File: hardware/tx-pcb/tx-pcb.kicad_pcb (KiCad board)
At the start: 2 copper layers, 61 parts, among them J1 Conn_To_J1, J2 Conn_To_J2, J3 BLIO, J4 Conn_01x05, J5 Conn_01x04, SW1 BOOT0, SW2 RESET, SW3 BTN1, SW4 BTN2, SW5 BTN3, SW6 BTN4, SW7 BTN5, U1 USBLC6-2SC6, U2 STM32WB55CEUx, X1 CS11336-32M, X2 ABS07-32.768KHZ-1-T

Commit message: progressed on hardware design
progressed on hardware design. completed most of the layout. waiting for pitch of the sx1262 and decision on switching regulator.
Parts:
- C16, C20, C21, C22, C23, C24, R10, R11, R12, R13, R14, SW3, SW4, SW5, SW6, SW7: moved to B.Cu
- R9: moved to F.Cu
- moved C20 134.4 mm to (186.8, 114.4)
- moved SW3 128.9 mm to (184.2, 113.8), turned to 180 degrees
- moved USB1 127.5 mm to (126.0, 90.2), turned to -90 degrees
- moved R2 120.4 mm to (131.9, 90.2), turned to -90 degrees
- moved R10 119.7 mm to (183.0, 111.0), turned to 0 degrees
- moved R1 117.8 mm to (131.4, 86.0), turned to 0 degrees
- moved U1 116.7 mm to (134.9, 90.0), turned to 0 degrees
- moved C21 114.8 mm to (186.8, 129.1)
- moved D1 112.4 mm to (135.0, 86.0), turned to 180 degrees
- moved SW4 109.6 mm to (184.2, 128.8), turned to 180 degrees
- moved J3 104.1 mm to (146.5, 65.0)
- moved R11 100.7 mm to (183.8, 126.0), turned to 0 degrees
- moved C23 97.4 mm to (186.8, 98.9)
- moved L4 97.3 mm to (146.4, 73.2), turned to 90 degrees
- moved C15 95.4 mm to (148.9, 72.0), turned to 0 degrees
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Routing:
- net /BOOT0: track 0.00 -> 57.5 mm, vias 0 -> 2
- net /SWD_NSRT: track 0.00 -> 48.9 mm, vias 0 -> 1
- net /SWCLK: track 0.00 -> 31.1 mm
- net /SWDIO: track 0.00 -> 27.4 mm
- net /I2C1_SCL: track 2.96 -> 23.1 mm
- net /I2C1_SDA: track 2.60 -> 22.2 mm
- net /SX1262_RST: track 0.00 -> 12.5 mm
- net /SX1262_DIO1: track 0.00 -> 11.7 mm
- net /SPI_MOSI: track 0.00 -> 10.7 mm
- net /SP1_MISO: track 0.00 -> 9.91 mm
- net Net-(R5-Pad2): track 0.00 -> 9.57 mm
- net /SPI_SCK: track 0.00 -> 9.08 mm
- net /SX1262_NSS: track 0.00 -> 8.07 mm
- net /USB_DP: track 3.56 -> 10.1 mm
- net /USB_DM: track 3.56 -> 10.1 mm
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- added copper zone on B.Cu, net +3V3
- added copper zone on F.Cu, net +3V3
- added copper zone on In1.Cu, net GND
- added copper zone on In2.Cu, net GND
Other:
- board outline added: 83.4 x 79.1 mm
- copper layers 2 -> 4
- board text added: "BOOT"
- board text added: "RESET"
- board text added: "gnd"
- board text added: "rst"
- board text added: "scl"
- board text added: "sda"
- board text added: "swclk"
- board text added: "swdio"
- board text added: "vcc"

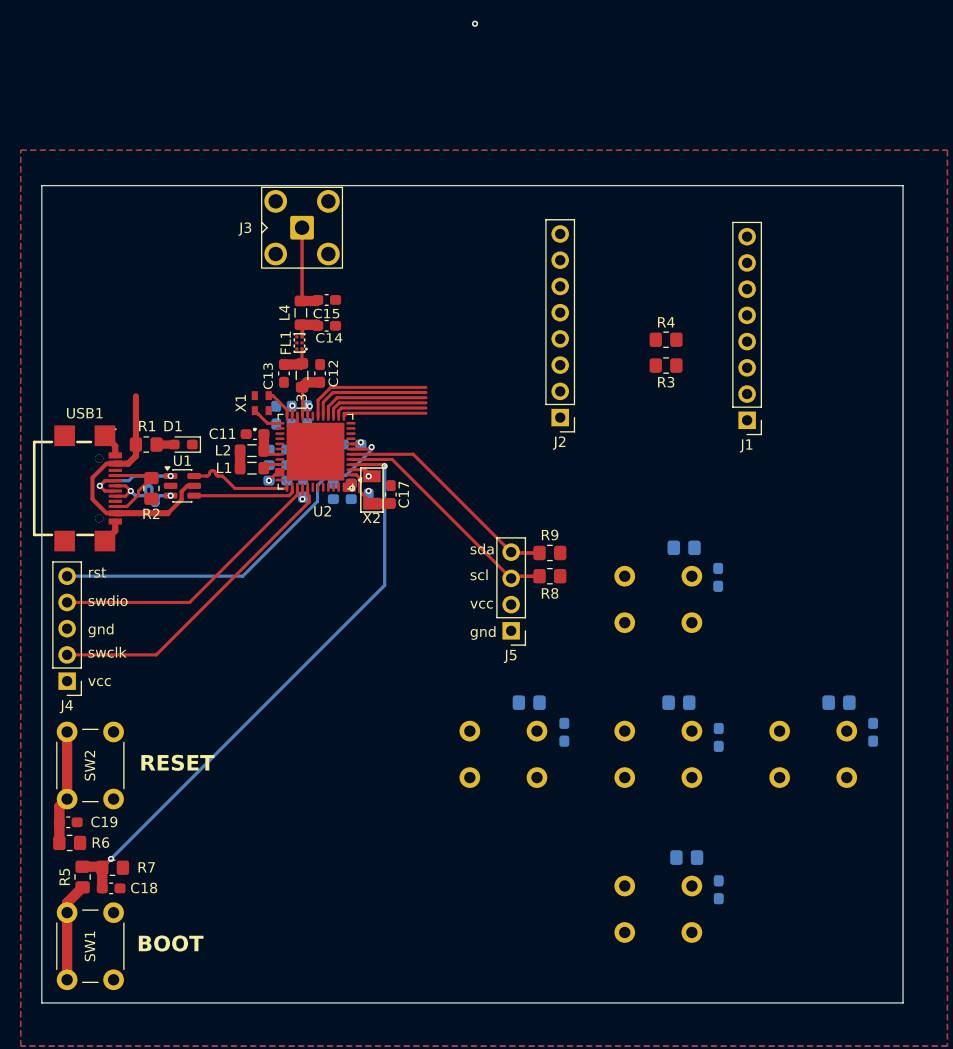
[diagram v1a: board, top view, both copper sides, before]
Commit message: worked on transmitter layout
updated transmitter schematic to use the sx1262 dev board over the chip
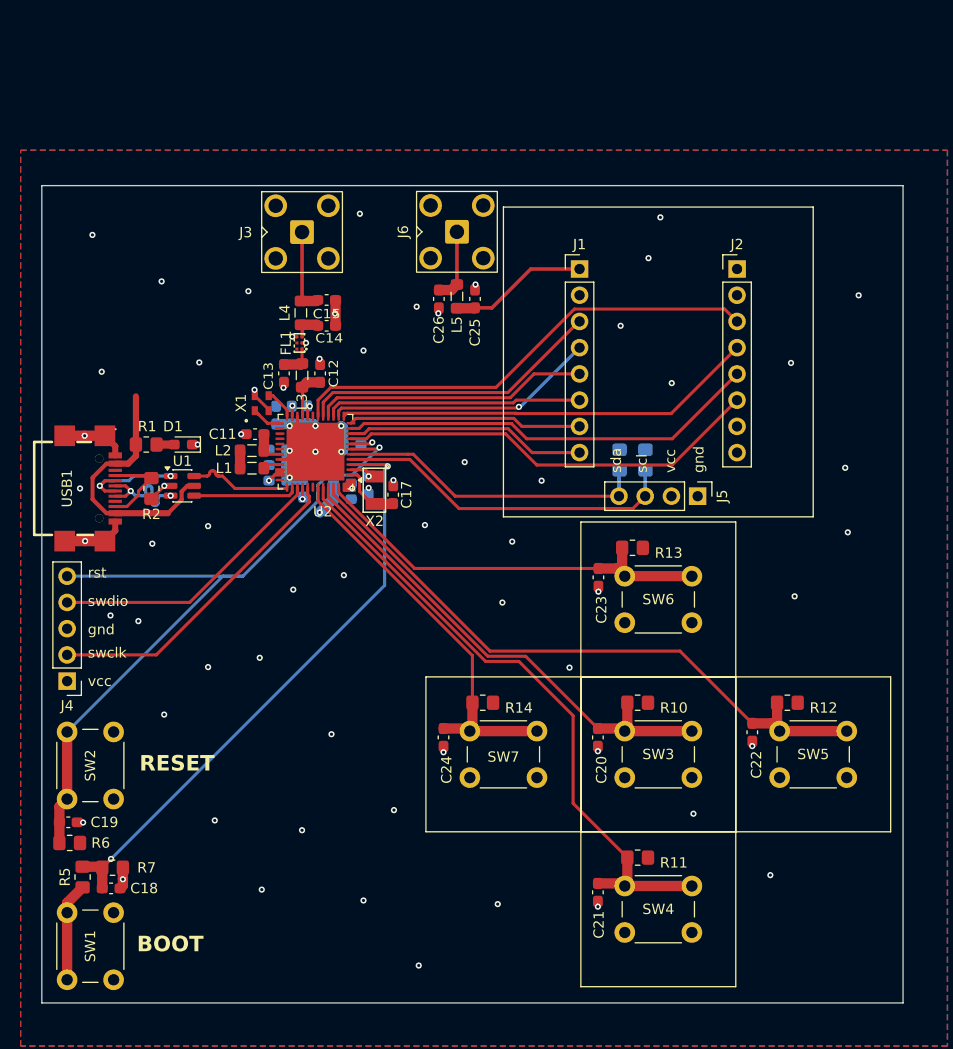
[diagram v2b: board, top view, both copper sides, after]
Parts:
- removed R3, R4: 0R, Resistor_SMD:R_0805_2012Metric_Pad1.20x1.40mm_HandSolder
- added C25: C, Capacitor_SMD:C_0603_1608Metric_Pad1.08x0.95mm_HandSolder, F.Cu at (163.2, 71.9)
- added C26: C, Capacitor_SMD:C_0603_1608Metric_Pad1.08x0.95mm_HandSolder, F.Cu at (159.8, 71.9)
- added J6: PWRO, Connector_Coaxial:SMA_BAT_Wireless_BWSMA-KWE-Z001, F.Cu at (161.5, 65.4)
- added L5: L, Inductor_SMD:L_0805_2012Metric_Pad1.05x1.20mm_HandSolder, F.Cu at (161.5, 71.7)
- C20, C21, C22, C23, C24, R10, R11, R12, R13, R14, SW3, SW4, SW5, SW6, SW7: moved to F.Cu
- R8, R9: moved to B.Cu
- USB1: footprint easyeda2kicad:USB-C-SMD_GT-USB-7047A -> rf-pwr-tx-library:USB-C-SMD_GT-USB-7047A
- moved C24 41.6 mm to (160.2, 114.4)
- moved SW7 36.5 mm to (162.8, 113.8), turned to 0 degrees
- moved R14 34.5 mm to (164.0, 111.0), turned to 180 degrees
- moved R12 25.0 mm to (193.5, 111.0), turned to 180 degrees
- moved SW5 23.5 mm to (192.8, 113.8), turned to 0 degrees
- moved J2 22.4 mm to (188.6, 69.0), turned to 0 degrees
- moved J5 22.3 mm to (184.8, 91.0), turned to -90 degrees
- moved J1 21.9 mm to (173.4, 69.0), turned to 0 degrees
- moved C22 18.2 mm to (190.1, 113.9)
- moved R8 14.6 mm to (179.8, 87.5), turned to -90 degrees
- moved C21 11.7 mm to (175.2, 129.4)
- moved C20 11.7 mm to (175.2, 114.4)
- moved C23 11.6 mm to (175.2, 98.9)
- moved R9 11.2 mm to (177.2, 87.5), turned to -90 degrees
- moved SW3 6.50 mm to (177.8, 113.8), turned to 0 degrees
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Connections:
- J1 pad 1: /SX1262_RFSW -> Net-(J1-Pin_1)
- J1 pad 2: /SX1262_RFSW# -> GND
- J1 pad 3: /SX1262_BUSY -> /SX1262_NSS
- J1 pad 4: unconnected-(J1-Pin_4-Pad4) -> /SPI_SCK
- J1 pad 5: +3V3 -> /SPI_MOSI
- J1 pad 6: +3V3 -> /SPI_MISO
- J1 pad 7: +3V3 -> /SX1262_RST
- J1 pad 8: GND -> /SX1262_BUSY
- J2 pad 1: /SX1262_NSS -> GND
- J2 pad 2: /SPI_SCK -> GND
- J2 pad 3: Net-(J2-Pin_3) -> /SX1262_RFSW#
- J2 pad 4: Net-(J2-Pin_4) -> /SX1262_RFSW
- J2 pad 5: /SX1262_DIO1 -> /SX1262_DIO2
- J2 pad 6: /SX1262_RST -> /SX1262_DIO1
- J2 pad 7: unconnected-(J2-Pin_7-Pad7) -> GND
- J2 pad 8: GND -> +3V3
- U2 pad 10: /SX1262_RFSW -> /SX1262_BUSY
- U2 pad 11: /SX1262_RFSW# -> /SX1262_DIO2
- U2 pad 12: /SX1262_BUSY -> /SX1262_RST
- U2 pad 13: /SX1262_NSS -> /SX1262_RFSW
- U2 pad 15: /SP1_MISO -> /SPI_MISO
- U2 pad 17: /SX1262_DIO1 -> /SX1262_NSS
- U2 pad 18: /SX1262_RST -> /SX1262_RFSW#
- U2 pad 43: /BTN1 -> /BTN5
- U2 pad 45: /BTN3 -> /BTN1
- U2 pad 46: /BTN4 -> /BTN3
- U2 pad 47: /BTN5 -> /BTN4
- U2 pad 9: unconnected-(U2-PA0-Pad9) -> /SX1262_DIO1
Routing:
- net /BTN3: track 0.00 -> 62.8 mm
- net /BTN2: track 0.00 -> 62.0 mm
- net /BTN1: track 0.00 -> 48.7 mm
- net /SX1262_RFSW#: track 0.00 -> 46.3 mm
- net /BTN4: track 0.00 -> 40.9 mm
- net /SX1262_RFSW: track 0.00 -> 40.9 mm
- net /SX1262_DIO2: track 0.00 -> 40.8 mm
- net /BTN5: track 0.00 -> 39.1 mm
- net GND: track 9.10 -> 45.3 mm, vias 1 -> 47
- net /SX1262_DIO1: track 11.7 -> 41.4 mm
- net /SPI_MISO: track 0.00 -> 24.9 mm
- net /SWD_NSRT: track 48.9 -> 73.4 mm
- net /SX1262_BUSY: track 0.00 -> 23.3 mm
- net /SX1262_NSS: track 8.07 -> 29.4 mm
- net /SPI_SCK: track 9.08 -> 26.4 mm, vias 0 -> 1
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
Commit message: finished tx layout v1.0
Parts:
- added J7: Conn_01x02_Pin, Connector_PinHeader_2.54mm:PinHeader_1x02_P2.54mm_Vertical, F.Cu at (158.0, 135.2)
- added SW8: SW_SPDT, rf-pwr-tx-library:spdt_amazon, F.Cu at (146.8, 135.2)
- added U3: ~, rf-pwr-tx-library:TPS63070_board, B.Cu at (146.8, 114.2)
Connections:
- net Net-(U1-VBUS) renamed /VBUS
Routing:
- net /VBUS: track 24.9 -> 66.4 mm, vias 0 -> 2
- net /reg_in: track 0.00 -> 11.4 mm
- net Net-(J7-Pin_1): track 0.00 -> 6.55 mm
- net /SWDIO: track 27.4 -> 30.9 mm
